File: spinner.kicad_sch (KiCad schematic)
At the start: 39 parts, among them SW1 SW_SPDT, U1 SFH617A-3X006, U2 SFH617A-3X006, U3 SFH617A-3X006, U4 RS0102, U5 AP63205WU

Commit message: IDK.  Add the kitchen sink.
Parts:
- added C109, C110, C111, C112, C113, C114, C115, C201, C202, C203, C204, C205, C206, C207, C208, C209, C210, C211, C212, C213, C214, C215, C301, C302, C303, C304, C305, C306, C307, C308, C309, C310, C311, C312, C313, C314, C315: .1uF, Capacitor_SMD:C_0805_2012Metric_Pad1.18x1.45mm_HandSolder, symbol Device:C_Polarized
- added D109, D110, D111, D112, D113, D114, D115, D201, D202, D203, D204, D205, D206, D207, D208, D209, D210, D211, D212, D213, D214, D215, D301, D302, D303, D304, D305, D306, D307, D308, D309, D310, D311, D312, D313, D314, D315: APA102, LED_SMD:LED_RGB_5050-6, symbol LED:APA102
- BT1, BT2, BT3, BT4, BT5, BT6: footprint Battery:BatteryHolder_Keystone_2460_1xAA -> Library:Spinner_BatteryHolder_Keystone_2460_1xAA
- renumbered C5 to C101, C6 to C102, C7 to C103, C8 to C104, C9 to C105, C10 to C106, C11 to C107, C12 to C108, D1 to D101, D2 to D102, D3 to D103, D4 to D104, D5 to D105, D6 to D106, D7 to D107, D8 to D108
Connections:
- net +3V3: now also A1.14 (3V); no longer A1.13 (3V)
- net GND: now also A1.15 (GND), U2.2, C109.2, C110.2, C111.2, C112.2, C113.2, C114.2, C115.2, C201.2, C202.2, C203.2, C204.2, C205.2, C206.2, C207.2, C208.2, C209.2, C210.2, C211.2, C212.2, C213.2, C214.2, C215.2, C301.2, C302.2, C303.2, C304.2, C305.2, C306.2, C307.2, C308.2, C309.2, C310.2, C311.2, C312.2, C313.2, C314.2, C315.2, D109.3 (GND), D110.3 (GND), D111.3 (GND), D112.3 (GND), D113.3 (GND), D114.3 (GND), D115.3 (GND), D201.3 (GND), D202.3 (GND), D203.3 (GND), D204.3 (GND), D205.3 (GND), D206.3 (GND), D207.3 (GND), D208.3 (GND), D209.3 (GND), D210.3 (GND), D211.3 (GND), D212.3 (GND), D213.3 (GND), D214.3 (GND), D215.3 (GND), D301.3 (GND), D302.3 (GND), D303.3 (GND), D304.3 (GND), D305.3 (GND), D306.3 (GND), D307.3 (GND), D308.3 (GND), D309.3 (GND), D310.3 (GND), D311.3 (GND), D312.3 (GND), D313.3 (GND), D314.3 (GND), D315.3 (GND); no longer U1.2
- net GPIO_13: now also A1.13
- net GPIO_14: now also A1.11 (14)
- net OPTO_in_0: now also A1.8 (25)
- net OPTO_in_1: now also A1.9 (26)
- net OPTO_in_2: now also A1.10 (27)
- net VCC: now also A1.16 (VBat), C109.1, C110.1, C111.1, C112.1, C113.1, C114.1, C115.1, C201.1, C202.1, C203.1, C204.1, C205.1, C206.1, C207.1, C208.1, C209.1, C210.1, C211.1, C212.1, C213.1, C214.1, C215.1, C301.1, C302.1, C303.1, C304.1, C305.1, C306.1, C307.1, C308.1, C309.1, C310.1, C311.1, C312.1, C313.1, C314.1, C315.1, D109.4 (VCC), D110.4 (VCC), D111.4 (VCC), D112.4 (VCC), D113.4 (VCC), D114.4 (VCC), D115.4 (VCC), D201.4 (VCC), D202.4 (VCC), D203.4 (VCC), D204.4 (VCC), D205.4 (VCC), D206.4 (VCC), D207.4 (VCC), D208.4 (VCC), D209.4 (VCC), D210.4 (VCC), D211.4 (VCC), D212.4 (VCC), D213.4 (VCC), D214.4 (VCC), D215.4 (VCC), D301.4 (VCC), D302.4 (VCC), D303.4 (VCC), D304.4 (VCC), D305.4 (VCC), D306.4 (VCC), D307.4 (VCC), D308.4 (VCC), D309.4 (VCC), D310.4 (VCC), D311.4 (VCC), D312.4 (VCC), D313.4 (VCC), D314.4 (VCC), D315.4 (VCC); no longer A1.8 (V+)
- net at U3.1: now also U1.2; no longer U2.2
- net at D108.5 (CO): now also D109.2 (CI)
- net at D108.6 (DO): now also D109.1 (DI)
- net at C1.1, U5.2 (EN), U5.3 (IN): now also SW1.3 (C); no longer SW1.1 (A)
- new net: D205.6 (DO), D206.1 (DI)
- new net: D205.5 (CO), D206.2 (CI)
- new net: D206.5 (CO), D207.2 (CI)
- new net: D206.6 (DO), D207.1 (DI)
- new net: D204.6 (DO), D205.1 (DI)
- new net: D204.5 (CO), D205.2 (CI)
- new net: D313.6 (DO), D314.1 (DI)
- new net: D313.5 (CO), D314.2 (CI)
- new net: D314.5 (CO), D315.2 (CI)
- new net: D314.6 (DO), D315.1 (DI)
- new net: D201.5 (CO), D202.2 (CI)
- new net: D201.6 (DO), D202.1 (DI)
- new net: D207.5 (CO), D208.2 (CI)
- new net: D207.6 (DO), D208.1 (DI)
- new net: D303.6 (DO), D304.1 (DI)
- new net: D303.5 (CO), D304.2 (CI)
- new net: D304.5 (CO), D305.2 (CI)
- new net: D304.6 (DO), D305.1 (DI)
- new net: D301.5 (CO), D302.2 (CI)
- new net: D301.6 (DO), D302.1 (DI)
- new net: D312.6 (DO), D313.1 (DI)
- new net: D312.5 (CO), D313.2 (CI)
- new net: D208.6 (DO), D209.1 (DI)
- new net: D208.5 (CO), D209.2 (CI)
- new net: D209.5 (CO), D210.2 (CI)
- new net: D209.6 (DO), D210.1 (DI)
- new net: D203.6 (DO), D204.1 (DI)
- new net: D203.5 (CO), D204.2 (CI)
- new net: D210.6 (DO), D211.1 (DI)
- new net: D210.5 (CO), D211.2 (CI)
- new net: D211.5 (CO), D212.2 (CI)
- new net: D211.6 (DO), D212.1 (DI)
- new net: D109.5 (CO), D110.2 (CI)
- new net: D109.6 (DO), D110.1 (DI)
- new net: D305.5 (CO), D306.2 (CI)
- new net: D305.6 (DO), D306.1 (DI)
- new net: D214.6 (DO), D215.1 (DI)
- new net: D214.5 (CO), D215.2 (CI)
- new net: D202.6 (DO), D203.1 (DI)
- new net: D202.5 (CO), D203.2 (CI)
- new net: D306.5 (CO), D307.2 (CI)
- new net: D306.6 (DO), D307.1 (DI)
- new net: D310.6 (DO), D311.1 (DI)
- new net: D310.5 (CO), D311.2 (CI)
- new net: D311.5 (CO), D312.2 (CI)
- new net: D311.6 (DO), D312.1 (DI)
- new net: D212.5 (CO), D213.2 (CI)
- new net: D212.6 (DO), D213.1 (DI)
- new net: D111.6 (DO), D112.1 (DI)
- new net: D111.5 (CO), D112.2 (CI)
- new net: D112.5 (CO), D113.2 (CI)
- new net: D112.6 (DO), D113.1 (DI)
- new net: D213.6 (DO), D214.1 (DI)
- new net: D213.5 (CO), D214.2 (CI)
- new net: D113.5 (CO), D114.2 (CI)
- new net: D113.6 (DO), D114.1 (DI)
- new net: D307.5 (CO), D308.2 (CI)
- new net: D307.6 (DO), D308.1 (DI)
- new net: D308.5 (CO), D309.2 (CI)
- new net: D308.6 (DO), D309.1 (DI)
- new net: D114.5 (CO), D115.2 (CI)
- new net: D114.6 (DO), D115.1 (DI)
- new net: D110.6 (DO), D111.1 (DI)
- new net: D110.5 (CO), D111.2 (CI)
- new net: D302.6 (DO), D303.1 (DI)
- new net: D302.5 (CO), D303.2 (CI)
- new net: D309.6 (DO), D310.1 (DI)
- new net: D309.5 (CO), D310.2 (CI)
- new net CO_1: D115.5 (CO), D301.2 (CI)
- new net CO_3: D201.2 (CI), D315.5 (CO)
- new net DO_1: D115.6 (DO), D301.1 (DI)
- new net DO_3: D201.1 (DI), D315.6 (DO)
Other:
- moved on the sheet: I2, U4

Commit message: Update things.  Next checkin.
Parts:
- added H101, H102, H103, H104, H105, H106, H107, H108, H109: MountingHole, MountingHole:MountingHole_3mm, symbol Mechanical:MountingHole
- renumbered A1 to A101, BT1 to BT101, BT2 to BT102, BT3 to BT103, BT4 to BT104, BT5 to BT105, BT6 to BT106, C1 to C101, C2 to C102, C3 to C103, C4 to C104, C301 to C105, C101 to C106, C201 to C107, C302 to C108, C102 to C109, C202 to C110, C303 to C111, C103 to C112, C203 to C113, C304 to C114, C104 to C115, C204 to C116, C305 to C117, C105 to C118, C205 to C119, C306 to C120, C106 to C121, C206 to C122, C307 to C123, C107 to C124, C207 to C125, C308 to C126, C108 to C127, C208 to C128, C309 to C129, C109 to C130, C209 to C131, C310 to C132, C110 to C133, C210 to C134, C311 to C135, C111 to C136, C211 to C137, C312 to C138, C112 to C139, C212 to C140, C313 to C141, C113 to C142, C213 to C143, C314 to C144, C114 to C145, C214 to C146, C315 to C147, C115 to C148, C215 to C149, D301 to D101, D101 to D102, D201 to D103, D302 to D104, D102 to D105, D202 to D106, D303 to D107, D103 to D108, D203 to D109, D304 to D110, D104 to D111, D204 to D112, D305 to D113, D105 to D114, D205 to D115, D306 to D116, D106 to D117, D206 to D118, D307 to D119, D107 to D120, D207 to D121, D308 to D122, D108 to D123, D208 to D124, D309 to D125, D109 to D126, D209 to D127, D310 to D128, D110 to D129, D210 to D130, D311 to D131, D111 to D132, D211 to D133, D312 to D134, D112 to D135, D212 to D136, D313 to D137, D113 to D138, D213 to D139, D314 to D140, D114 to D141, D214 to D142, D315 to D143, D115 to D144, D215 to D145, I1 to I101, I2 to I102, L1 to L101, R1 to R101, R2 to R102, R3 to R103, SW1 to SW101, U1 to U101, U2 to U102, U3 to U103, U4 to U104, U5 to U105

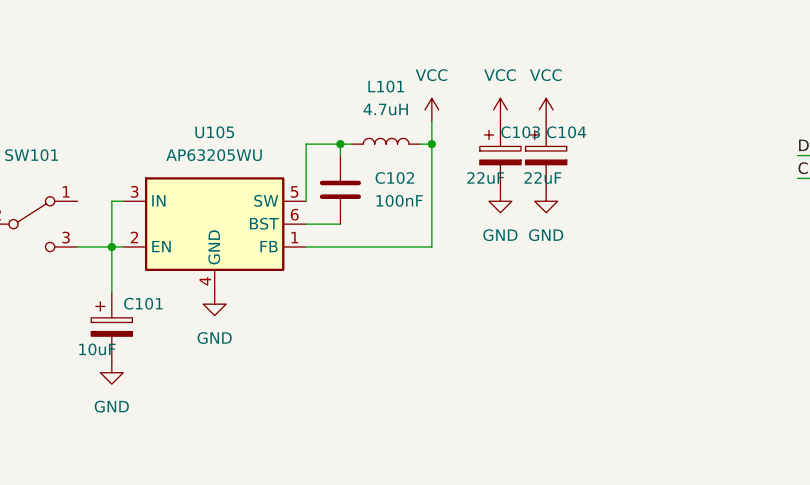
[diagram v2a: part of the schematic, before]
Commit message: Adding the BOM and more backups and updates to kicad files.
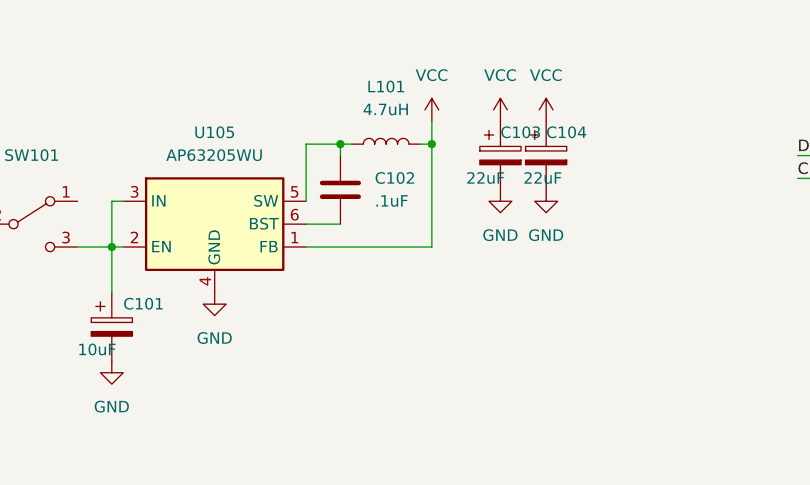
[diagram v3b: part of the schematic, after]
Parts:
- C102: value 100nF -> .1uF
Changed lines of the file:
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@@
       (effects (font (size 1.27 1.27)) (justify left))
     )
-    (property "Value" "100nF" (id 1) (at 109.22 34.2899 0)
+    (property "Value" ".1uF" (id 1) (at 109.22 34.2899 0)
       (effects (font (size 1.27 1.27)) (justify left))
     )
@@
     )
     (path "/be96cdf2-70c9-421a-9b6e-1e352656c531"
-      (reference "C102") (unit 1) (value "100nF") (footprint "Capacitor_SMD:C_0805_2012Metric_Pad1.18x1.45mm_HandSolder")
+      (reference "C102") (unit 1) (value ".1uF") (footprint "Capacitor_SMD:C_0805_2012Metric_Pad1.18x1.45mm_HandSolder")
     )
     (path "/584fa1fc-1f61-4536-94c7-a3b2dc85ecba"

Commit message: Updated schematic and things.  For spin 2.  And board layout.
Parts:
- added TP1: GND, TestPoint:TestPoint_Pad_D2.5mm, symbol Connector:TestPoint
- added TP2: 3v3, TestPoint:TestPoint_Pad_D2.5mm, symbol Connector:TestPoint
- added TP3: Opto_1, TestPoint:TestPoint_Pad_D2.5mm, symbol Connector:TestPoint
- added TP4: VCC, TestPoint:TestPoint_Pad_D2.5mm, symbol Connector:TestPoint
- added TP5: BATT, TestPoint:TestPoint_Pad_D2.5mm, symbol Connector:TestPoint
- added TP6: Opto_0, TestPoint:TestPoint_Pad_D2.5mm, symbol Connector:TestPoint
- added TP7: DI, TestPoint:TestPoint_Pad_D2.5mm, symbol Connector:TestPoint
- added TP8: CI, TestPoint:TestPoint_Pad_D2.5mm, symbol Connector:TestPoint
- added TP9: Opto_2, TestPoint:TestPoint_Pad_D2.5mm, symbol Connector:TestPoint
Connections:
- net +3V3: now also R101.1, R102.1, R103.1, TP2.1
- net +BATT: now also TP5.1
- net CI: now also TP8.1
- net DI: now also TP7.1
- net GND: now also U101.4, U102.4, U103.4, TP1.1; no longer U101.3, U102.3, U103.3
- net OPTO_in_0: now also U101.3, TP6.1; no longer U101.4
- net OPTO_in_1: now also U102.3, TP3.1; no longer U102.4
- net OPTO_in_2: now also U103.3, TP9.1; no longer U103.4
- net VCC: now also TP4.1; no longer R101.1, R102.1, R103.1

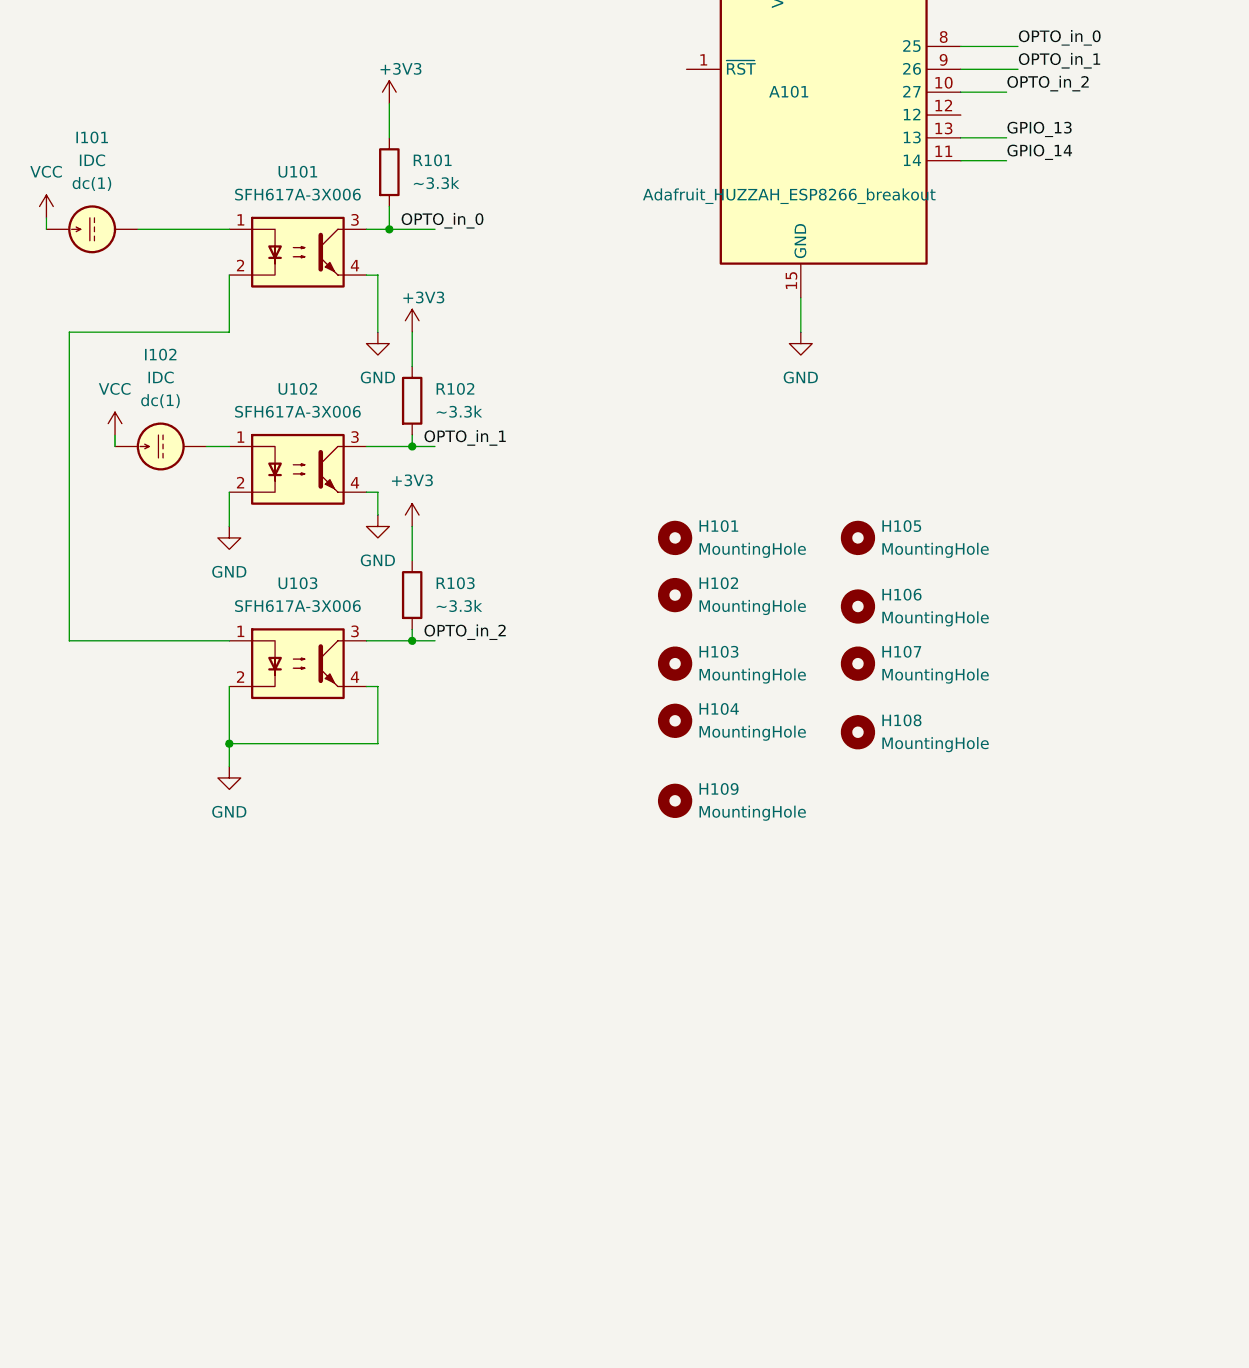
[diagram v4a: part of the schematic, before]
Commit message: Adding things: SD card, resistor pack, routing.  Totally done.
Issue: HKZ-563
Changelog: No Functional Change.
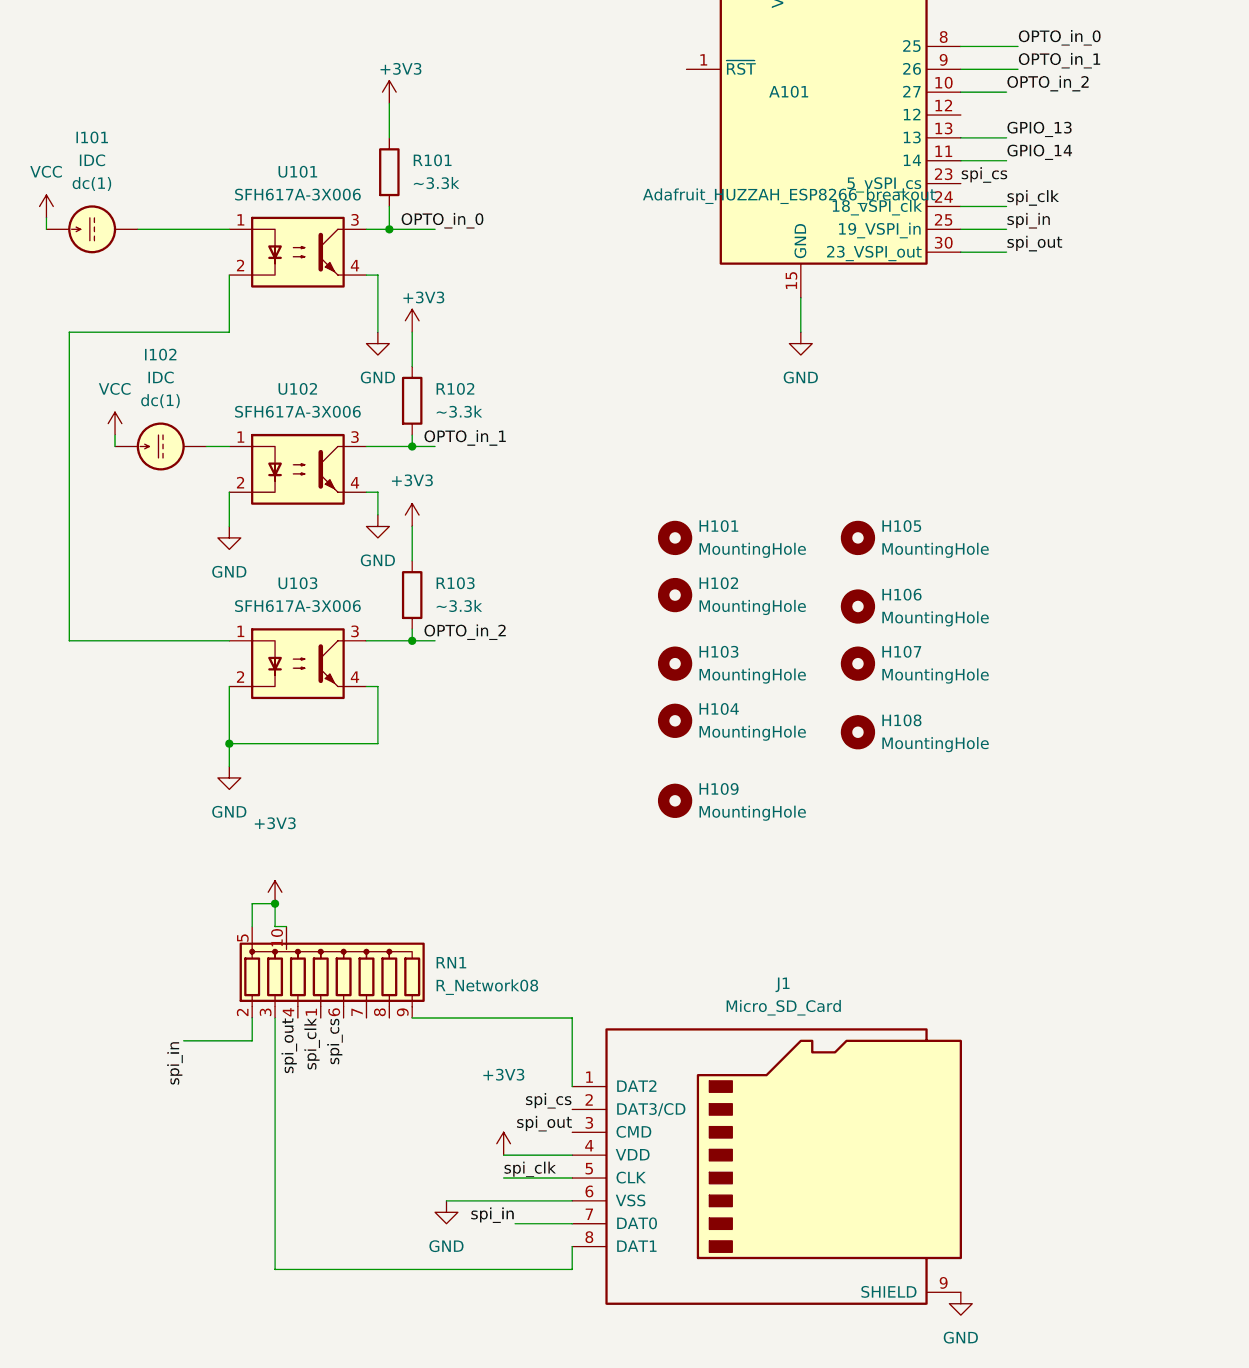
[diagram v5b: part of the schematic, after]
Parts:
- added J1: Micro_SD_Card, Connector_Card:microSD_HC_Hirose_DM3AT-SF-PEJM5, symbol Connector:Micro_SD_Card
- added RN1: R_Network08, Resistor_SMD:R_Array_Convex_5x1206, symbol Device:R_Network08
- U101, U102: footprint Package_DIP:DIP-4_W10.16mm -> Library:MULTI_PART_THRU_BEAM
- U103: footprint Package_DIP:DIP-4_W10.16mm -> Library:tcrt1000
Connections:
- net +3V3: now also J1.4 (VDD), RN1.10 (common), RN1.5 (common)
- net GND: now also J1.6 (VSS), J1.9 (SHIELD)
- new net: J1.8 (DAT1), RN1.3 (R2)
- new net: J1.1 (DAT2), RN1.9 (R8)
- new net spi_clk: A101.24 (18_vSPI_clk), J1.5 (CLK), RN1.1 (R4)
- new net spi_cs: A101.23 (5_vSPI_cs), J1.2 (DAT3/CD), RN1.6 (R5)
- new net spi_in: A101.25 (19_VSPI_in), J1.7 (DAT0), RN1.2 (R1)
- new net spi_out: A101.30 (23_VSPI_out), J1.3 (CMD), RN1.4 (R3)

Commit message: Start the mini version of the spinner.
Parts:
- removed BT104, BT105, BT106: Battery_Cell, Library:Spinner_BatteryHolder_Keystone_2460_1xAA, symbol Device:Battery_Cell
- removed C105, C106, C107, C108, C109, C110, C111, C112, C113, C114, C115, C116, C117, C118, C119, C120, C121, C122, C123, C124, C125, C126, C127, C128, C129, C130, C131, C132, C133, C134, C135, C136, C137, C138, C139, C140, C141, C142, C143, C144, C145, C146, C147, C148, C149: .1uF, Capacitor_SMD:C_0805_2012Metric_Pad1.18x1.45mm_HandSolder, symbol Device:C_Polarized
- added D101: APA102, Library:SK9822-hakz, symbol LED:APA102
- D0: renamed from D102; footprint LED_SMD:LED_RGB_5050-6 -> Library:SK9822-hakz
- D102: renamed from D105; footprint LED_SMD:LED_RGB_5050-6 -> Library:SK9822-hakz
- D103: renamed from D108; footprint LED_SMD:LED_RGB_5050-6 -> Library:SK9822-hakz
- D104: renamed from D111; footprint LED_SMD:LED_RGB_5050-6 -> Library:SK9822-hakz
- D105: renamed from D114; footprint LED_SMD:LED_RGB_5050-6 -> Library:SK9822-hakz
- D106: renamed from D117; footprint LED_SMD:LED_RGB_5050-6 -> Library:SK9822-hakz
- D107: renamed from D120; footprint LED_SMD:LED_RGB_5050-6 -> Library:SK9822-hakz
- D108: renamed from D123; footprint LED_SMD:LED_RGB_5050-6 -> Library:SK9822-hakz
- D109: renamed from D126; footprint LED_SMD:LED_RGB_5050-6 -> Library:SK9822-hakz
- D110: renamed from D129; footprint LED_SMD:LED_RGB_5050-6 -> Library:SK9822-hakz
- D111: renamed from D132; footprint LED_SMD:LED_RGB_5050-6 -> Library:SK9822-hakz
- D112: renamed from D135; footprint LED_SMD:LED_RGB_5050-6 -> Library:SK9822-hakz
- D113: renamed from D138; footprint LED_SMD:LED_RGB_5050-6 -> Library:SK9822-hakz
- D114: renamed from D141; footprint LED_SMD:LED_RGB_5050-6 -> Library:SK9822-hakz
- D115: renamed from D144; footprint LED_SMD:LED_RGB_5050-6 -> Library:SK9822-hakz
- D201: renamed from D101; footprint LED_SMD:LED_RGB_5050-6 -> Library:SK9822-hakz
- D202: renamed from D104; footprint LED_SMD:LED_RGB_5050-6 -> Library:SK9822-hakz
- D203: renamed from D107; footprint LED_SMD:LED_RGB_5050-6 -> Library:SK9822-hakz
- D204: renamed from D110; footprint LED_SMD:LED_RGB_5050-6 -> Library:SK9822-hakz
- D205: renamed from D113; footprint LED_SMD:LED_RGB_5050-6 -> Library:SK9822-hakz
- D206: renamed from D116; footprint LED_SMD:LED_RGB_5050-6 -> Library:SK9822-hakz
- D207: renamed from D119; footprint LED_SMD:LED_RGB_5050-6 -> Library:SK9822-hakz
- D208: renamed from D122; footprint LED_SMD:LED_RGB_5050-6 -> Library:SK9822-hakz
- D209: renamed from D125; footprint LED_SMD:LED_RGB_5050-6 -> Library:SK9822-hakz
- D210: renamed from D128; footprint LED_SMD:LED_RGB_5050-6 -> Library:SK9822-hakz
- D211: renamed from D131; footprint LED_SMD:LED_RGB_5050-6 -> Library:SK9822-hakz
- D212: renamed from D134; footprint LED_SMD:LED_RGB_5050-6 -> Library:SK9822-hakz
- D213: renamed from D137; footprint LED_SMD:LED_RGB_5050-6 -> Library:SK9822-hakz
- D214: renamed from D140; footprint LED_SMD:LED_RGB_5050-6 -> Library:SK9822-hakz
- D215: renamed from D143; footprint LED_SMD:LED_RGB_5050-6 -> Library:SK9822-hakz
- D301: renamed from D103; footprint LED_SMD:LED_RGB_5050-6 -> Library:SK9822-hakz
- D302: renamed from D106; footprint LED_SMD:LED_RGB_5050-6 -> Library:SK9822-hakz
- D303: renamed from D109; footprint LED_SMD:LED_RGB_5050-6 -> Library:SK9822-hakz
- D304: renamed from D112; footprint LED_SMD:LED_RGB_5050-6 -> Library:SK9822-hakz
- D305: renamed from D115; footprint LED_SMD:LED_RGB_5050-6 -> Library:SK9822-hakz
- D306: renamed from D118; footprint LED_SMD:LED_RGB_5050-6 -> Library:SK9822-hakz
- D307: renamed from D121; footprint LED_SMD:LED_RGB_5050-6 -> Library:SK9822-hakz
- D308: renamed from D124; footprint LED_SMD:LED_RGB_5050-6 -> Library:SK9822-hakz
- D309: renamed from D127; footprint LED_SMD:LED_RGB_5050-6 -> Library:SK9822-hakz
- D310: renamed from D130; footprint LED_SMD:LED_RGB_5050-6 -> Library:SK9822-hakz
- D311: renamed from D133; footprint LED_SMD:LED_RGB_5050-6 -> Library:SK9822-hakz
- D312: renamed from D136; footprint LED_SMD:LED_RGB_5050-6 -> Library:SK9822-hakz
- D313: renamed from D139; footprint LED_SMD:LED_RGB_5050-6 -> Library:SK9822-hakz
- D314: renamed from D142; footprint LED_SMD:LED_RGB_5050-6 -> Library:SK9822-hakz
- D315: renamed from D145; footprint LED_SMD:LED_RGB_5050-6 -> Library:SK9822-hakz
- renumbered A101 to A1, BT101 to BT1, BT102 to BT2, BT103 to BT3, C103 to C1, C104 to C2, C102 to C3, C101 to C4, H101 to H1, H105 to H2, H102 to H3, H106 to H4, H103 to H5, H107 to H6, H104 to H7, H108 to H8, H109 to H9, I101 to I1, I102 to I2, L101 to L1, R101 to R1, R102 to R2, R103 to R3, SW101 to SW1, TP8 to TP1, TP1 to TP2, TP2 to TP3, TP7 to TP5, TP9 to TP6, TP3 to TP7, TP6 to TP8, TP5 to TP9, U105 to U1, U104 to U2, U101 to U3, U102 to U4, U103 to U5
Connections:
- net GND: now also BT3.2 (-), D101.3 (GND)
- net VCC: now also D101.4 (VCC)
- net at D102.1 (DI): now also D101.6 (DO); no longer D0.6 (DO)
- net at D102.2 (CI): now also D101.5 (CO); no longer D0.5 (CO)
- new net: D0.5 (CO), D101.2 (CI)
- new net: D0.6 (DO), D101.1 (DI)
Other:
- moved on the sheet: D0, D201, D202, D203, D204, D205, D206, D207, D208, D209, D210, D211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
